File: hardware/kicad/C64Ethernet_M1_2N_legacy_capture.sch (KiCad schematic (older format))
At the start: 7 parts, among them J1 C64_USERPORT, J2 RJ45_MAGJACK, U1 LC4032V-5TN48C, U2 W5500, U3 REG_3V3, X1 25MHz

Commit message: hardware: align M1.2N schematic nets with symbol pins
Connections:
- net labels added: DEVICE_IRQ
- net labels removed: 3V3, GND
- wire segments 30 -> 29
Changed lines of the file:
@@
 Sheet 1 1
 Title "C64Ethernet M1.2N engineering capture"
-Date "2026-09-15"
+Date "2026-09-16"
 Rev "M1.2N"
 Comp "Ploos-AS"
 Comment1 "Legacy capture prepared for KiCad migration"
 Comment2 "C64 User Port -> LC4032V -> W5500 -> Ethernet"
-Comment3 "Not ERC qualified"
+Comment3 "ERC qualification in progress"
 Comment4 "Do not manufacture from this revision"
 $EndDescr
@@
 U 1 1 10000001
 P 1800 3500
-F 0 "J1" H 1800 4550 50  0000 C CNN
+F 0 "J1" H 1800 4550 50 0000 C CNN
 F 1 "C64_USERPORT" H 1800 4450 50 0000 C CNN
 	1    1800 3500
@@
 $EndComp
 Wire Wire Line
-	2300 3000 4000 3000
+	2500 3000 3900 3000
 Wire Wire Line
-	2300 3100 4000 3100
+	2500 3100 3900 3100
 Wire Wire Line
-	2300 3200 4000 3200
+	2500 3200 3900 3200
 Wire Wire Line
-	2300 3300 4000 3300
+	2500 3300 3900 3300
 Wire Wire Line
-	2300 3400 4000 3400
+	2500 3400 3900 3400
 Wire Wire Line
-	2300 3500 4000 3500
+	2500 3500 3900 3500
 Wire Wire Line
-	2300 3600 4000 3600
+	2500 3600 3900 3600
 Wire Wire Line
-	2300 3700 4000 3700
+	2500 3700 3900 3700
 Wire Wire Line
-	2300 3900 4000 3900
+	2500 3900 3900 3900
 Wire Wire Line
-	5400 3000 7000 3000
+	2500 4000 3900 4000
 Wire Wire Line
-	5400 3100 7000 3100
+	5500 3000 6900 3000
 Wire Wire Line
-	5400 3200 7000 3200
+	5500 3100 6900 3100
 Wire Wire Line
-	5400 3300 7000 3300
+	5500 3200 6900 3200
 Wire Wire Line
-	5400 3400 7000 3400
+	5500 3300 6900 3300
 Wire Wire Line
-	5400 3500 7000 3500
+	5500 3400 6900 3400
 Wire Wire Line
-	5400 3600 7000 3600
+	5500 3500 6900 3500
 Wire Wire Line
-	5400 3700 7000 3700
+	8500 3100 9000 3100
 Wire Wire Line
-	8400 3000 9700 3000
+	8500 3200 9000 3200
 Wire Wire Line
-	8400 3100 9700 3100
+	8500 3400 9000 3400
 Wire Wire Line
-	8400 3200 9700 3200
+	8500 3500 9000 3500
 Wire Wire Line
-	8400 3300 9700 3300
+	9450 3200 9700 3200
 Wire Wire Line
-	8400 3400 9700 3400
+	9450 3300 9700 3300
 Wire Wire Line
-	8400 3500 9700 3500
+	9450 3500 9700 3500
 Wire Wire Line
-	8400 3600 9700 3600
+	9450 3600 9700 3600
 Wire Wire Line
-	8400 3700 9700 3700
+	4250 5500 4100 5500
 Wire Wire Line
-	4400 5600 4200 5600
-Wire Wire Line
-	5000 5600 5200 5600
+	5150 5500 5300 5500
 Wire Wire Line
 	6650 5400 6500 5400
@@
 Wire Wire Line
 	7750 5400 7900 5400
-Text Label 2400 3000 0 50 ~ 0
+Text Label 2600 3000 0 50 ~ 0
 PB0
-Text Label 2400 3100 0 50 ~ 0
+Text Label 2600 3100 0 50 ~ 0
 PB1
-Text Label 2400 3200 0 50 ~ 0
+Text Label 2600 3200 0 50 ~ 0
 PB2
-Text Label 2400 3300 0 50 ~ 0
+Text Label 2600 3300 0 50 ~ 0
 PB3
-Text Label 2400 3400 0 50 ~ 0
+Text Label 2600 3400 0 50 ~ 0
 PB4
-Text Label 2400 3500 0 50 ~ 0
+Text Label 2600 3500 0 50 ~ 0
 PB5
-Text Label 2400 3600 0 50 ~ 0
+Text Label 2600 3600 0 50 ~ 0
 PB6
-Text Label 2400 3700 0 50 ~ 0
+Text Label 2600 3700 0 50 ~ 0
 PB7
-Text Label 2400 3900 0 50 ~ 0
+Text Label 2600 3900 0 50 ~ 0
 PA2_HOST_STROBE
-Text Label 5450 3000 0 50 ~ 0
+Text Label 2600 4000 0 50 ~ 0
+DEVICE_IRQ
+Text Label 5600 3000 0 50 ~ 0
 SCLK
-Text Label 5450 3100 0 50 ~ 0
+Text Label 5600 3100 0 50 ~ 0
 MOSI
-Text Label 5450 3200 0 50 ~ 0
+Text Label 5600 3200 0 50 ~ 0
 MISO
-Text Label 5450 3300 0 50 ~ 0
+Text Label 5600 3300 0 50 ~ 0
 SCSn
-Text Label 5450 3400 0 50 ~ 0
+Text Label 5600 3400 0 50 ~ 0
 INTn
-Text Label 5450 3500 0 50 ~ 0
+Text Label 5600 3500 0 50 ~ 0
 RSTn
-Text Label 5450 3600 0 50 ~ 0
-3V3
-Text Label 5450 3700 0 50 ~ 0
-GND
-Text Label 8500 3000 0 50 ~ 0
+Text Label 8600 3100 0 50 ~ 0
 TXP
-Text Label 8500 3100 0 50 ~ 0
+Text Label 8600 3200 0 50 ~ 0
 TXN
-Text Label 8500 3200 0 50 ~ 0
+Text Label 8600 3400 0 50 ~ 0
 RXP
-Text Label 8500 3300 0 50 ~ 0
+Text Label 8600 3500 0 50 ~ 0
+RXN
+Text Label 9550 3200 0 50 ~ 0
+TXP
+Text Label 9550 3300 0 50 ~ 0
+TXN
+Text Label 9550 3500 0 50 ~ 0
+RXP
+Text Label 9550 3600 0 50 ~ 0
 RXN
 Text Label 6500 5400 2 50 ~ 0

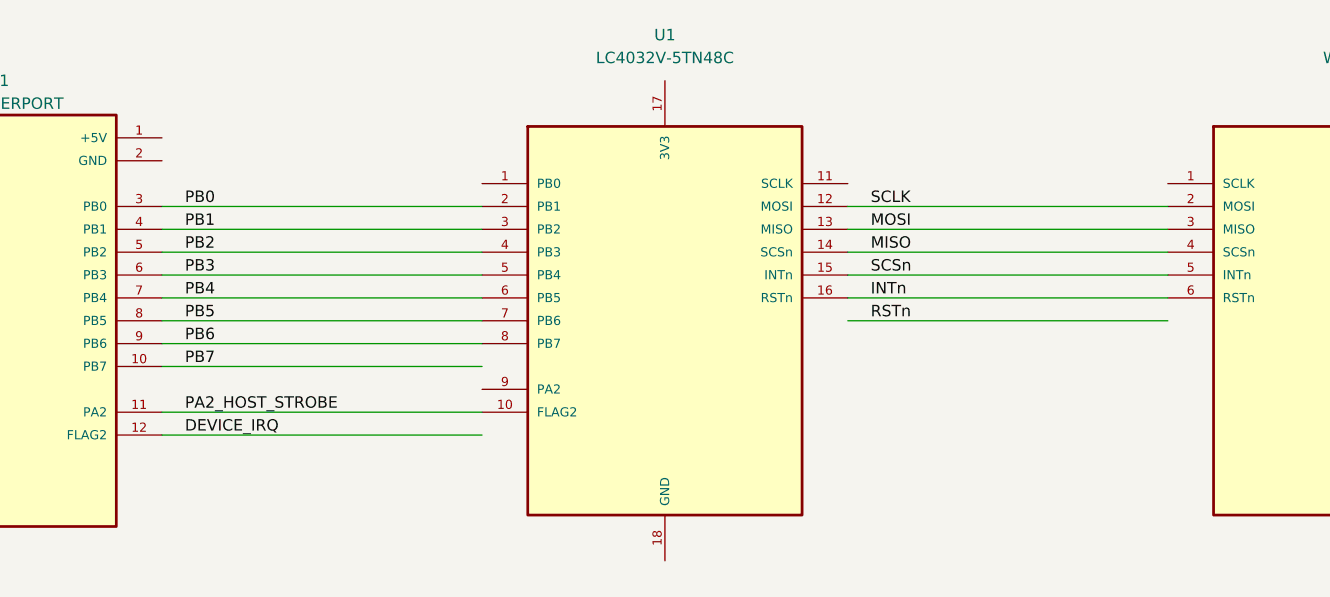
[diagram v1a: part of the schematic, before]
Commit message: hardware: align legacy schematic wires with symbol pins
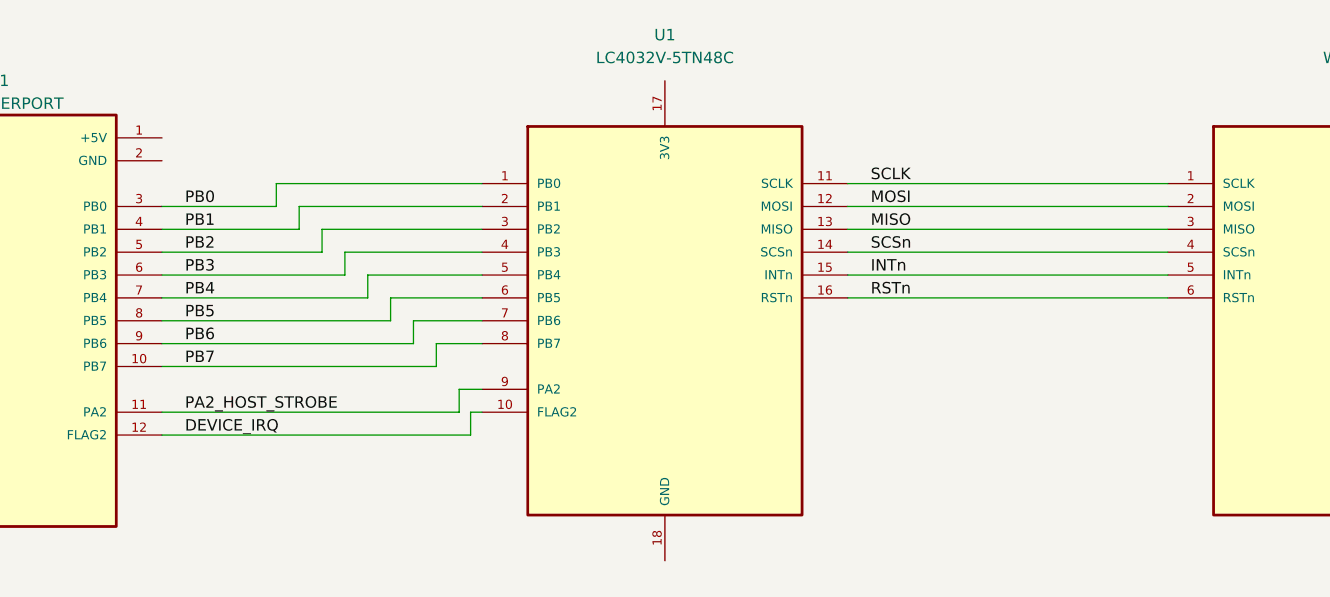
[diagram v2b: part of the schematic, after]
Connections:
- wire segments 29 -> 49
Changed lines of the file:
@@
 $EndComp
 Wire Wire Line
-	2500 3000 3900 3000
+	2500 3000 3000 3000
 Wire Wire Line
-	2500 3100 3900 3100
+	3000 3000 3000 2900
 Wire Wire Line
-	2500 3200 3900 3200
+	3000 2900 3900 2900
 Wire Wire Line
-	2500 3300 3900 3300
+	2500 3100 3100 3100
 Wire Wire Line
-	2500 3400 3900 3400
+	3100 3100 3100 3000
 Wire Wire Line
-	2500 3500 3900 3500
+	3100 3000 3900 3000
 Wire Wire Line
-	2500 3600 3900 3600
+	2500 3200 3200 3200
 Wire Wire Line
-	2500 3700 3900 3700
+	3200 3200 3200 3100
 Wire Wire Line
-	2500 3900 3900 3900
+	3200 3100 3900 3100
 Wire Wire Line
-	2500 4000 3900 4000
+	2500 3300 3300 3300
+Wire Wire Line
+	3300 3300 3300 3200
+Wire Wire Line
+	3300 3200 3900 3200
+Wire Wire Line
+	2500 3400 3400 3400
+Wire Wire Line
+	3400 3400 3400 3300
+Wire Wire Line
+	3400 3300 3900 3300
+Wire Wire Line
+	2500 3500 3500 3500
+Wire Wire Line
+	3500 3500 3500 3400
+Wire Wire Line
+	3500 3400 3900 3400
+Wire Wire Line
+	2500 3600 3600 3600
+Wire Wire Line
+	3600 3600 3600 3500
+Wire Wire Line
+	3600 3500 3900 3500
+Wire Wire Line
+	2500 3700 3700 3700
+Wire Wire Line
+	3700 3700 3700 3600
+Wire Wire Line
+	3700 3600 3900 3600
+Wire Wire Line
+	2500 3900 3800 3900
+Wire Wire Line
+	3800 3900 3800 3800
+Wire Wire Line
+	3800 3800 3900 3800
+Wire Wire Line
+	2500 4000 3850 4000
+Wire Wire Line
+	3850 4000 3850 3900
+Wire Wire Line
+	3850 3900 3900 3900
+Wire Wire Line
+	5500 2900 6900 2900
 Wire Wire Line
 	5500 3000 6900 3000
@@
 Wire Wire Line
 	5500 3400 6900 3400
-Wire Wire Line
-	5500 3500 6900 3500
 Wire Wire Line
 	8500 3100 9000 3100
@@
 Text Label 2600 4000 0 50 ~ 0
 DEVICE_IRQ
+Text Label 5600 2900 0 50 ~ 0
+SCLK
 Text Label 5600 3000 0 50 ~ 0
-SCLK
+MOSI
 Text Label 5600 3100 0 50 ~ 0
-MOSI
+MISO
 Text Label 5600 3200 0 50 ~ 0
-MISO
+SCSn
 Text Label 5600 3300 0 50 ~ 0
-SCSn
+INTn
 Text Label 5600 3400 0 50 ~ 0
-INTn
-Text Label 5600 3500 0 50 ~ 0
 RSTn
 Text Label 8600 3100 0 50 ~ 0

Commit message: fix: attach schematic net labels directly to symbol pins
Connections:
- net labels added: GND
- wire segments 49 -> 0
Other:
- note added: "M1.2N capture: labels are anchored directly to symbol pins for deterministic KiCad migration/ERC connectivity."
- note removed: "M1.2N capture: symbolized engineering source for migration to native .kicad_sch."
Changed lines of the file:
@@
 W5500 ETHERNET
 Text Notes 900 6750 0 60 ~ 12
-M1.2N capture: symbolized engineering source for migration to native .kicad_sch.
+M1.2N capture: labels are anchored directly to symbol pins for deterministic KiCad migration/ERC connectivity.
 $Comp
 L C64_USERPORT J1
@@
 	1 0 0 -1
 $EndComp
-Wire Wire Line
-	2500 3000 3000 3000
-Wire Wire Line
-	3000 3000 3000 2900
-Wire Wire Line
-	3000 2900 3900 2900
-Wire Wire Line
-	2500 3100 3100 3100
-Wire Wire Line
-	3100 3100 3100 3000
-Wire Wire Line
-	3100 3000 3900 3000
-Wire Wire Line
-	2500 3200 3200 3200
-Wire Wire Line
-	3200 3200 3200 3100
-Wire Wire Line
-	3200 3100 3900 3100
-Wire Wire Line
-	2500 3300 3300 3300
-Wire Wire Line
-	3300 3300 3300 3200
-Wire Wire Line
-	3300 3200 3900 3200
-Wire Wire Line
-	2500 3400 3400 3400
-Wire Wire Line
-	3400 3400 3400 3300
-Wire Wire Line
-	3400 3300 3900 3300
-Wire Wire Line
-	2500 3500 3500 3500
-Wire Wire Line
-	3500 3500 3500 3400
-Wire Wire Line
-	3500 3400 3900 3400
-Wire Wire Line
-	2500 3600 3600 3600
-Wire Wire Line
-	3600 3600 3600 3500
-Wire Wire Line
-	3600 3500 3900 3500
-Wire Wire Line
-	2500 3700 3700 3700
-Wire Wire Line
-	3700 3700 3700 3600
-Wire Wire Line
-	3700 3600 3900 3600
-Wire Wire Line
-	2500 3900 3800 3900
-Wire Wire Line
-	3800 3900 3800 3800
-Wire Wire Line
-	3800 3800 3900 3800
-Wire Wire Line
-	2500 4000 3850 4000
-Wire Wire Line
-	3850 4000 3850 3900
-Wire Wire Line
-	3850 3900 3900 3900
-Wire Wire Line
-	5500 2900 6900 2900
-Wire Wire Line
-	5500 3000 6900 3000
-Wire Wire Line
-	5500 3100 6900 3100
-Wire Wire Line
-	5500 3200 6900 3200
-Wire Wire Line
-	5500 3300 6900 3300
-Wire Wire Line
-	5500 3400 6900 3400
-Wire Wire Line
-	8500 3100 9000 3100
-Wire Wire Line
-	8500 3200 9000 3200
-Wire Wire Line
-	8500 3400 9000 3400
-Wire Wire Line
-	8500 3500 9000 3500
-Wire Wire Line
-	9450 3200 9700 3200
-Wire Wire Line
-	9450 3300 9700 3300
-Wire Wire Line
-	9450 3500 9700 3500
-Wire Wire Line
-	9450 3600 9700 3600
-Wire Wire Line
-	4250 5500 4100 5500
-Wire Wire Line
-	5150 5500 5300 5500
-Wire Wire Line
-	6650 5400 6500 5400
-Wire Wire Line
-	6950 5400 7450 5400
-Wire Wire Line
-	7750 5400 7900 5400
-Text Label 2600 3000 0 50 ~ 0
+Text Label 2500 3000 0 50 ~ 0
 PB0
-Text Label 2600 3100 0 50 ~ 0
+Text Label 2500 3100 0 50 ~ 0
 PB1
-Text Label 2600 3200 0 50 ~ 0
+Text Label 2500 3200 0 50 ~ 0
 PB2
-Text Label 2600 3300 0 50 ~ 0
+Text Label 2500 3300 0 50 ~ 0
 PB3
-Text Label 2600 3400 0 50 ~ 0
+Text Label 2500 3400 0 50 ~ 0
 PB4
-Text Label 2600 3500 0 50 ~ 0
+Text Label 2500 3500 0 50 ~ 0
 PB5
-Text Label 2600 3600 0 50 ~ 0
+Text Label 2500 3600 0 50 ~ 0
 PB6
-Text Label 2600 3700 0 50 ~ 0
+Text Label 2500 3700 0 50 ~ 0
 PB7
-Text Label 2600 3900 0 50 ~ 0
+Text Label 2500 3900 0 50 ~ 0
 PA2_HOST_STROBE
-Text Label 2600 4000 0 50 ~ 0
+Text Label 2500 4000 0 50 ~ 0
 DEVICE_IRQ
-Text Label 5600 2900 0 50 ~ 0
+Text Label 3900 2900 2 50 ~ 0
+PB0
+Text Label 3900 3000 2 50 ~ 0
+PB1
+Text Label 3900 3100 2 50 ~ 0
+PB2
+Text Label 3900 3200 2 50 ~ 0
+PB3
+Text Label 3900 3300 2 50 ~ 0
+PB4
+Text Label 3900 3400 2 50 ~ 0
+PB5
+Text Label 3900 3500 2 50 ~ 0
+PB6
+Text Label 3900 3600 2 50 ~ 0
+PB7
+Text Label 3900 3800 2 50 ~ 0
+PA2_HOST_STROBE
+Text Label 3900 3900 2 50 ~ 0
+DEVICE_IRQ
+Text Label 5500 2900 0 50 ~ 0
 SCLK
-Text Label 5600 3000 0 50 ~ 0
+Text Label 5500 3000 0 50 ~ 0
 MOSI
-Text Label 5600 3100 0 50 ~ 0
+Text Label 5500 3100 0 50 ~ 0
 MISO
-Text Label 5600 3200 0 50 ~ 0
+Text Label 5500 3200 0 50 ~ 0
 SCSn
-Text Label 5600 3300 0 50 ~ 0
+Text Label 5500 3300 0 50 ~ 0
 INTn
-Text Label 5600 3400 0 50 ~ 0
+Text Label 5500 3400 0 50 ~ 0
 RSTn
-Text Label 8600 3100 0 50 ~ 0
+Text Label 6900 2900 2 50 ~ 0
+SCLK
+Text Label 6900 3000 2 50 ~ 0
+MOSI
+Text Label 6900 3100 2 50 ~ 0
+MISO
+Text Label 6900 3200 2 50 ~ 0
+SCSn
+Text Label 6900 3300 2 50 ~ 0
+INTn
+Text Label 6900 3400 2 50 ~ 0
+RSTn
+Text Label 8500 2900 0 50 ~ 0
+EXRES1
+Text Label 8500 3100 0 50 ~ 0
 TXP
-Text Label 8600 3200 0 50 ~ 0
+Text Label 8500 3200 0 50 ~ 0
 TXN
-Text Label 8600 3400 0 50 ~ 0
+Text Label 8500 3400 0 50 ~ 0
 RXP
-Text Label 8600 3500 0 50 ~ 0
+Text Label 8500 3500 0 50 ~ 0
 RXN
-Text Label 9550 3200 0 50 ~ 0
+Text Label 9450 3200 2 50 ~ 0
 TXP
-Text Label 9550 3300 0 50 ~ 0
+Text Label 9450 3300 2 50 ~ 0
 TXN
-Text Label 9550 3500 0 50 ~ 0
+Text Label 9450 3500 2 50 ~ 0
 RXP
-Text Label 9550 3600 0 50 ~ 0
+Text Label 9450 3600 2 50 ~ 0
 RXN
-Text Label 6500 5400 2 50 ~ 0
+Text Label 6650 5400 2 50 ~ 0
 EXRES1
-Text Label 7900 5400 0 50 ~ 0
+Text Label 6950 5400 0 50 ~ 0
+GND
+Text Label 7450 5400 2 50 ~ 0
+OSC_RETURN
+Text Label 7750 5400 0 50 ~ 0
 OSC_RETURN
 $EndSCHEMATC

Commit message: fix: isolate remaining ERC dangling labels with outward stubs
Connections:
- wire segments 0 -> 23
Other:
- note added: "M1.2N capture: direct labels retained where ERC passes; short outward stubs isolate remaining migrated dangling-label cases."
- note removed: "M1.2N capture: labels are anchored directly to symbol pins for deterministic KiCad migration/ERC connectivity."
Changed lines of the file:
@@
 W5500 ETHERNET
 Text Notes 900 6750 0 60 ~ 12
-M1.2N capture: labels are anchored directly to symbol pins for deterministic KiCad migration/ERC connectivity.
+M1.2N capture: direct labels retained where ERC passes; short outward stubs isolate remaining migrated dangling-label cases.
 $Comp
 L C64_USERPORT J1
@@
 	1 0 0 -1
 $EndComp
-Text Label 2500 3000 0 50 ~ 0
+Wire Wire Line
+	2500 3000 2600 3000
+Wire Wire Line
+	2500 3600 2600 3600
+Wire Wire Line
+	2500 3900 2600 3900
+Wire Wire Line
+	2500 4000 2600 4000
+Wire Wire Line
+	3900 3000 3800 3000
+Wire Wire Line
+	3900 3100 3800 3100
+Wire Wire Line
+	3900 3200 3800 3200
+Wire Wire Line
+	3900 3300 3800 3300
+Wire Wire Line
+	3900 3400 3800 3400
+Wire Wire Line
+	3900 3600 3800 3600
+Wire Wire Line
+	5500 3100 5600 3100
+Wire Wire Line
+	6900 2900 6800 2900
+Wire Wire Line
+	6900 3000 6800 3000
+Wire Wire Line
+	6900 3200 6800 3200
+Wire Wire Line
+	6900 3300 6800 3300
+Wire Wire Line
+	6900 3400 6800 3400
+Wire Wire Line
+	6950 5400 7050 5400
+Wire Wire Line
+	8500 2900 8600 2900
+Wire Wire Line
+	8500 3200 8600 3200
+Wire Wire Line
+	8500 3400 8600 3400
+Wire Wire Line
+	8500 3500 8600 3500
+Wire Wire Line
+	7450 5400 7350 5400
+Wire Wire Line
+	9450 3200 9350 3200
+Text Label 2600 3000 0 50 ~ 0
 PB0
 Text Label 2500 3100 0 50 ~ 0
@@
 Text Label 2500 3500 0 50 ~ 0
 PB5
-Text Label 2500 3600 0 50 ~ 0
+Text Label 2600 3600 0 50 ~ 0
 PB6
 Text Label 2500 3700 0 50 ~ 0
 PB7
-Text Label 2500 3900 0 50 ~ 0
+Text Label 2600 3900 0 50 ~ 0
 PA2_HOST_STROBE
-Text Label 2500 4000 0 50 ~ 0
+Text Label 2600 4000 0 50 ~ 0
 DEVICE_IRQ
 Text Label 3900 2900 2 50 ~ 0
 PB0
-Text Label 3900 3000 2 50 ~ 0
+Text Label 3800 3000 2 50 ~ 0
 PB1
-Text Label 3900 3100 2 50 ~ 0
+Text Label 3800 3100 2 50 ~ 0
 PB2
-Text Label 3900 3200 2 50 ~ 0
+Text Label 3800 3200 2 50 ~ 0
 PB3
-Text Label 3900 3300 2 50 ~ 0
+Text Label 3800 3300 2 50 ~ 0
 PB4
-Text Label 3900 3400 2 50 ~ 0
+Text Label 3800 3400 2 50 ~ 0
 PB5
 Text Label 3900 3500 2 50 ~ 0
 PB6
-Text Label 3900 3600 2 50 ~ 0
+Text Label 3800 3600 2 50 ~ 0
 PB7
 Text Label 3900 3800 2 50 ~ 0
@@
 Text Label 5500 3000 0 50 ~ 0
 MOSI
-Text Label 5500 3100 0 50 ~ 0
+Text Label 5600 3100 0 50 ~ 0
 MISO
 Text Label 5500 3200 0 50 ~ 0
@@
 Text Label 5500 3400 0 50 ~ 0
 RSTn
-Text Label 6900 2900 2 50 ~ 0
+Text Label 6800 2900 2 50 ~ 0
 SCLK
-Text Label 6900 3000 2 50 ~ 0
+Text Label 6800 3000 2 50 ~ 0
 MOSI
 Text Label 6900 3100 2 50 ~ 0
 MISO
-Text Label 6900 3200 2 50 ~ 0
+Text Label 6800 3200 2 50 ~ 0
 SCSn
-Text Label 6900 3300 2 50 ~ 0
+Text Label 6800 3300 2 50 ~ 0
 INTn
-Text Label 6900 3400 2 50 ~ 0
+Text Label 6800 3400 2 50 ~ 0
 RSTn
-Text Label 8500 2900 0 50 ~ 0
+Text Label 8600 2900 0 50 ~ 0
 EXRES1
 Text Label 8500 3100 0 50 ~ 0
 TXP
-Text Label 8500 3200 0 50 ~ 0
+Text Label 8600 3200 0 50 ~ 0
 TXN
-Text Label 8500 3400 0 50 ~ 0
+Text Label 8600 3400 0 50 ~ 0
 RXP
-Text Label 8500 3500 0 50 ~ 0
+Text Label 8600 3500 0 50 ~ 0
 RXN
-Text Label 9450 3200 2 50 ~ 0
+Text Label 9350 3200 2 50 ~ 0
 TXP
 Text Label 9450 3300 2 50 ~ 0
@@
 Text Label 6650 5400 2 50 ~ 0
 EXRES1
-Text Label 6950 5400 0 50 ~ 0
+Text Label 7050 5400 0 50 ~ 0
 GND
-Text Label 7450 5400 2 50 ~ 0
+Text Label 7350 5400 2 50 ~ 0
 OSC_RETURN
 Text Label 7750 5400 0 50 ~ 0

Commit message: fix: restore best-known schematic label baseline
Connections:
- wire segments 23 -> 0
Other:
- note added: "M1.2N capture: labels are anchored directly to symbol pins for deterministic KiCad migration/ERC connectivity."
- note removed: "M1.2N capture: direct labels retained where ERC passes; short outward stubs isolate remaining migrated dangling-label cases."
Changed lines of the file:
@@
 W5500 ETHERNET
 Text Notes 900 6750 0 60 ~ 12
-M1.2N capture: direct labels retained where ERC passes; short outward stubs isolate remaining migrated dangling-label cases.
+M1.2N capture: labels are anchored directly to symbol pins for deterministic KiCad migration/ERC connectivity.
 $Comp
 L C64_USERPORT J1
@@
 	1 0 0 -1
 $EndComp
-Wire Wire Line
-	2500 3000 2600 3000
-Wire Wire Line
-	2500 3600 2600 3600
-Wire Wire Line
-	2500 3900 2600 3900
-Wire Wire Line
-	2500 4000 2600 4000
-Wire Wire Line
-	3900 3000 3800 3000
-Wire Wire Line
-	3900 3100 3800 3100
-Wire Wire Line
-	3900 3200 3800 3200
-Wire Wire Line
-	3900 3300 3800 3300
-Wire Wire Line
-	3900 3400 3800 3400
-Wire Wire Line
-	3900 3600 3800 3600
-Wire Wire Line
-	5500 3100 5600 3100
-Wire Wire Line
-	6900 2900 6800 2900
-Wire Wire Line
-	6900 3000 6800 3000
-Wire Wire Line
-	6900 3200 6800 3200
-Wire Wire Line
-	6900 3300 6800 3300
-Wire Wire Line
-	6900 3400 6800 3400
-Wire Wire Line
-	6950 5400 7050 5400
-Wire Wire Line
-	8500 2900 8600 2900
-Wire Wire Line
-	8500 3200 8600 3200
-Wire Wire Line
-	8500 3400 8600 3400
-Wire Wire Line
-	8500 3500 8600 3500
-Wire Wire Line
-	7450 5400 7350 5400
-Wire Wire Line
-	9450 3200 9350 3200
-Text Label 2600 3000 0 50 ~ 0
+Text Label 2500 3000 0 50 ~ 0
 PB0
 Text Label 2500 3100 0 50 ~ 0
@@
 Text Label 2500 3500 0 50 ~ 0
 PB5
-Text Label 2600 3600 0 50 ~ 0
+Text Label 2500 3600 0 50 ~ 0
 PB6
 Text Label 2500 3700 0 50 ~ 0
 PB7
-Text Label 2600 3900 0 50 ~ 0
+Text Label 2500 3900 0 50 ~ 0
 PA2_HOST_STROBE
-Text Label 2600 4000 0 50 ~ 0
+Text Label 2500 4000 0 50 ~ 0
 DEVICE_IRQ
 Text Label 3900 2900 2 50 ~ 0
 PB0
-Text Label 3800 3000 2 50 ~ 0
+Text Label 3900 3000 2 50 ~ 0
 PB1
-Text Label 3800 3100 2 50 ~ 0
+Text Label 3900 3100 2 50 ~ 0
 PB2
-Text Label 3800 3200 2 50 ~ 0
+Text Label 3900 3200 2 50 ~ 0
 PB3
-Text Label 3800 3300 2 50 ~ 0
+Text Label 3900 3300 2 50 ~ 0
 PB4
-Text Label 3800 3400 2 50 ~ 0
+Text Label 3900 3400 2 50 ~ 0
 PB5
 Text Label 3900 3500 2 50 ~ 0
 PB6
-Text Label 3800 3600 2 50 ~ 0
+Text Label 3900 3600 2 50 ~ 0
 PB7
 Text Label 3900 3800 2 50 ~ 0
@@
 Text Label 5500 3000 0 50 ~ 0
 MOSI
-Text Label 5600 3100 0 50 ~ 0
+Text Label 5500 3100 0 50 ~ 0
 MISO
 Text Label 5500 3200 0 50 ~ 0
@@
 Text Label 5500 3400 0 50 ~ 0
 RSTn
-Text Label 6800 2900 2 50 ~ 0
+Text Label 6900 2900 2 50 ~ 0
 SCLK
-Text Label 6800 3000 2 50 ~ 0
+Text Label 6900 3000 2 50 ~ 0
 MOSI
 Text Label 6900 3100 2 50 ~ 0
 MISO
-Text Label 6800 3200 2 50 ~ 0
+Text Label 6900 3200 2 50 ~ 0
 SCSn
-Text Label 6800 3300 2 50 ~ 0
+Text Label 6900 3300 2 50 ~ 0
 INTn
-Text Label 6800 3400 2 50 ~ 0
+Text Label 6900 3400 2 50 ~ 0
 RSTn
-Text Label 8600 2900 0 50 ~ 0
+Text Label 8500 2900 0 50 ~ 0
 EXRES1
 Text Label 8500 3100 0 50 ~ 0
 TXP
-Text Label 8600 3200 0 50 ~ 0
+Text Label 8500 3200 0 50 ~ 0
 TXN
-Text Label 8600 3400 0 50 ~ 0
+Text Label 8500 3400 0 50 ~ 0
 RXP
-Text Label 8600 3500 0 50 ~ 0
+Text Label 8500 3500 0 50 ~ 0
 RXN
-Text Label 9350 3200 2 50 ~ 0
+Text Label 9450 3200 2 50 ~ 0
 TXP
 Text Label 9450 3300 2 50 ~ 0
@@
 Text Label 6650 5400 2 50 ~ 0
 EXRES1
-Text Label 7050 5400 0 50 ~ 0
+Text Label 6950 5400 0 50 ~ 0
 GND
-Text Label 7350 5400 2 50 ~ 0
+Text Label 7450 5400 2 50 ~ 0
 OSC_RETURN
 Text Label 7750 5400 0 50 ~ 0
